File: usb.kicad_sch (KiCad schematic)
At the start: 8 parts, among them J2 USB_C_Receptacle_USB2.0

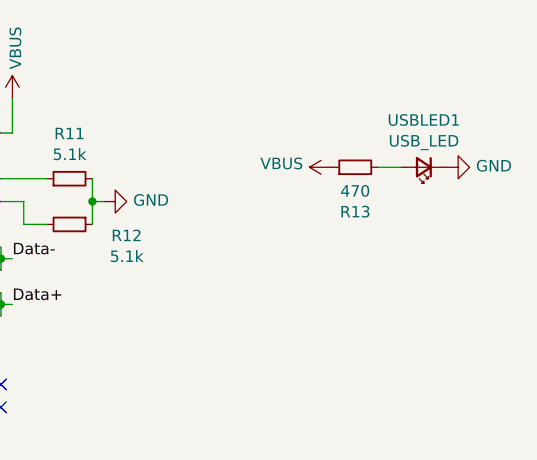
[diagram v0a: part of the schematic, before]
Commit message: implemented fixes that were changed for ordering of nimbus flight electronics, tidied up layout and set up manufacturing constraints
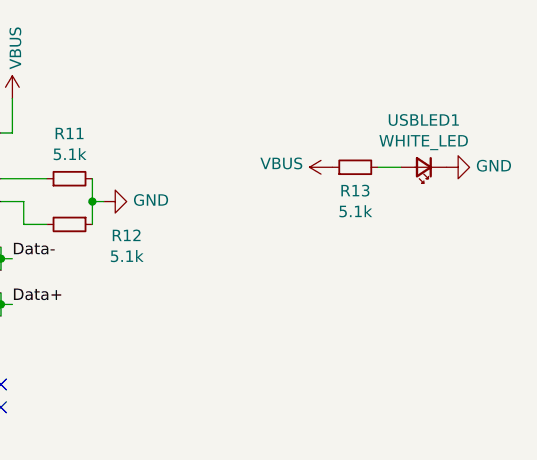
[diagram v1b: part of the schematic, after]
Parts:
- R13: value 470 -> 5.1k
- USBLED1: value USB_LED -> WHITE_LED
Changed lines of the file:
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@@
       (effects (font (size 1.27 1.27)))
     )
-    (property "Value" "USB_LED" (at 162.56 89.8144 0)
+    (property "Value" "WHITE_LED" (at 162.56 89.8144 0)
       (effects (font (size 1.27 1.27)))
     )
@@
   (symbol (lib_id "Device:R_Small") (at 154.94 92.71 90) (unit 1)
     (in_bom yes) (on_board yes) (dnp no)
-    (property "Reference" "R13" (at 154.94 97.6884 90)
+    (property "Reference" "R13" (at 154.94 95.3516 90)
       (effects (font (size 1.27 1.27)))
     )
-    (property "Value" "470" (at 154.94 95.377 90)
+    (property "Value" "5.1k" (at 154.94 97.663 90)
       (effects (font (size 1.27 1.27)))
     )

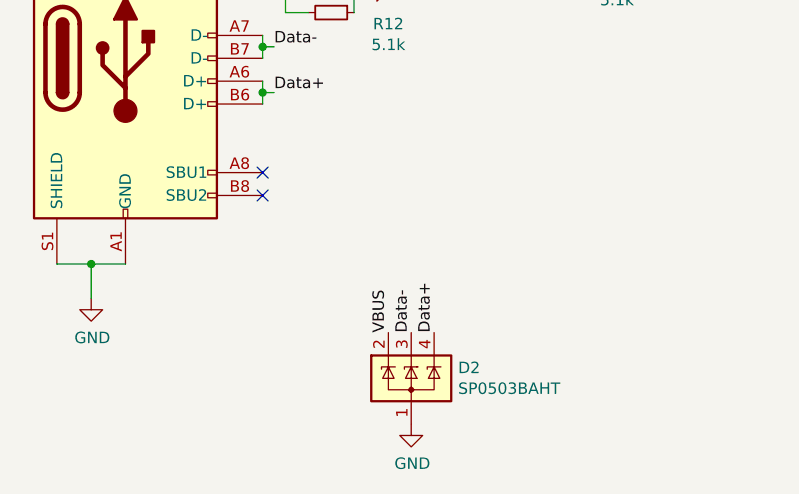
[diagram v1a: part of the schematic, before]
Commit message: Added CAN LEDs and some general fixes noticed over the year
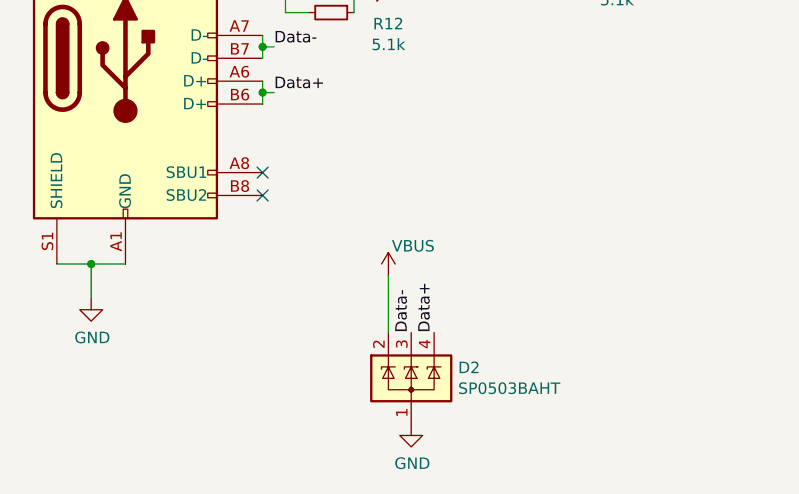
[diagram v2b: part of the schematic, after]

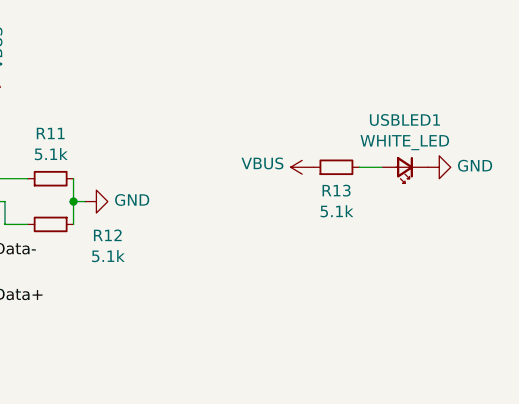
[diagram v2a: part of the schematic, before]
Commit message: Fixed LED footprints assigned as resistors, added gitignore for locks and backups
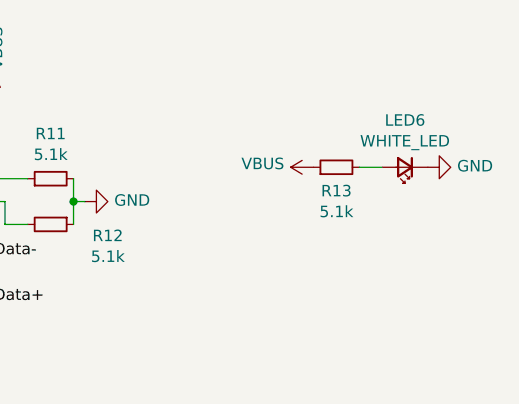
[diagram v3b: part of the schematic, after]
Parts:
- LED6: renamed from USBLED1; footprint Resistor_SMD:R_0402_1005Metric -> LED_SMD:LED_0402_1005Metric
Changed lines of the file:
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@@
 	(label "Data+"
 		(at 134.62 134.62 90)
-		(fields_autoplaced yes)
 		(effects
 			(font
@@
 	(label "Data+"
 		(at 44.45 104.14 0)
-		(fields_autoplaced yes)
 		(effects
 			(font
@@
 	(label "Data-"
 		(at 44.45 99.06 0)
-		(fields_autoplaced yes)
 		(effects
 			(font
@@
 	(label "Data-"
 		(at 132.08 134.62 90)
-		(fields_autoplaced yes)
 		(effects
 			(font
@@
 	(label "Data-"
 		(at 116.84 102.87 0)
-		(fields_autoplaced yes)
 		(effects
 			(font
@@
 	(label "Data+"
 		(at 116.84 107.95 0)
-		(fields_autoplaced yes)
 		(effects
 			(font
@@
 		(shape bidirectional)
 		(at 44.45 99.06 180)
-		(fields_autoplaced yes)
 		(effects
 			(font
@@
 		(shape bidirectional)
 		(at 44.45 104.14 180)
-		(fields_autoplaced yes)
 		(effects
 			(font
@@
 			)
 		)
-		(property "Description" ""
+		(property "Description" "Power symbol creates a global label with name \"GND\" , ground"
 			(at 127 96.52 0)
 			(effects
@@
 			)
 		)
-		(property "Description" ""
+		(property "Description" "Resistor, small symbol"
 			(at 123.19 99.06 0)
 			(effects
@@
 			)
 		)
-		(property "Description" ""
+		(property "Description" "Resistor, small symbol"
 			(at 123.19 93.98 0)
 			(effects
@@
 			)
 		)
-		(property "Description" ""
+		(property "Description" "Power symbol creates a global label with name \"GND\" , ground"
 			(at 96.52 130.81 0)
 			(effects
@@
 			)
 		)
-		(property "Description" ""
+		(property "Description" "Power symbol creates a global label with name \"GND\" , ground"
 			(at 132.08 144.78 0)
 			(effects
@@
 			)
 		)
-		(property "Description" ""
+		(property "Description" "TVS Diode Array, 5.5V Standoff, 3 Channels, SOT-143 package"
 			(at 132.08 139.7 0)
 			(effects
@@
 			)
 		)
-		(property "Description" ""
+		(property "Description" "Power symbol creates a global label with name \"VBUS\""
 			(at 116.84 85.09 0)
 			(effects
@@
 			)
 		)
-		(property "Description" ""
+		(property "Description" "test point"
 			(at 52.07 99.06 0)
 			(effects
@@
 			)
 		)
-		(property "Description" ""
+		(property "Description" "test point"
 			(at 52.07 104.14 0)
 			(effects
@@
 		(on_board yes)
 		(dnp no)
-		(property "Reference" "USBLED1"
+		(property "Reference" "LED6"
 			(at 162.56 87.503 0)
 			(effects
@@
 			)
 		)
-		(property "Footprint" "Resistor_SMD:R_0402_1005Metric"
+		(property "Footprint" "LED_SMD:LED_0402_1005Metric"
 			(at 162.56 92.71 90)
 			(effects
@@
 			)
 		)
-		(property "Description" ""
+		(property "Description" "Light emitting diode, small symbol"
 			(at 162.56 92.71 0)
 			(effects
@@
 			(project "RicardoTemplate"
 				(path "/7db990e4-92e1-4f99-b4d2-435bbec1ba83/00000000-0000-0000-0000-000061925999"
-					(reference "USBLED1")
+					(reference "LED6")
 					(unit 1)
 				)
@@
 			)
 		)
-		(property "Description" ""
+		(property "Description" "Resistor, small symbol"
 			(at 154.94 92.71 0)
 			(effects
@@
 			)
 		)
-		(property "Description" ""
+		(property "Description" "Power symbol creates a global label with name \"GND\" , ground"
 			(at 165.1 92.71 0)
 			(effects
@@
 			)
 		)
-		(property "Description" ""
+		(property "Description" "Power symbol creates a global label with name \"VBUS\""
 			(at 152.4 92.71 0)
 			(effects
@@
 			)
 		)
-		(property "Description" ""
+		(property "Description" "Power symbol creates a global label with name \"VBUS\""
 			(at 129.54 128.27 0)
 			(effects

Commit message: Fixed some footprint assignments, tidies up layout
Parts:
- J2: footprint Connector_USB:USB_C_Receptacle_Palconn_UTC16-G -> iclr:USB_C_Receptacle_Palconn_UTC16-G
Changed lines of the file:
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@@
 (kicad_sch
-	(version 20231120)
+	(version 20250114)
 	(generator "eeschema")
-	(generator_version "8.0")
+	(generator_version "9.0")
 	(paper "A4")
 	(junction
@@
 			)
 		)
-		(property "Footprint" "Connector_USB:USB_C_Receptacle_Palconn_UTC16-G"
+		(property "Footprint" "iclr:USB_C_Receptacle_Palconn_UTC16-G"
 			(at 104.14 104.14 0)
 			(effects
